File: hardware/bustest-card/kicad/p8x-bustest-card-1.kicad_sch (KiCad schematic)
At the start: 8 parts, among them U1 MCP23S17, U2 MCP23S17, U3 MCP23S17, U4 MCP23S17, U5 MCP23S17, U6 74HCT244, U7 74HCT244

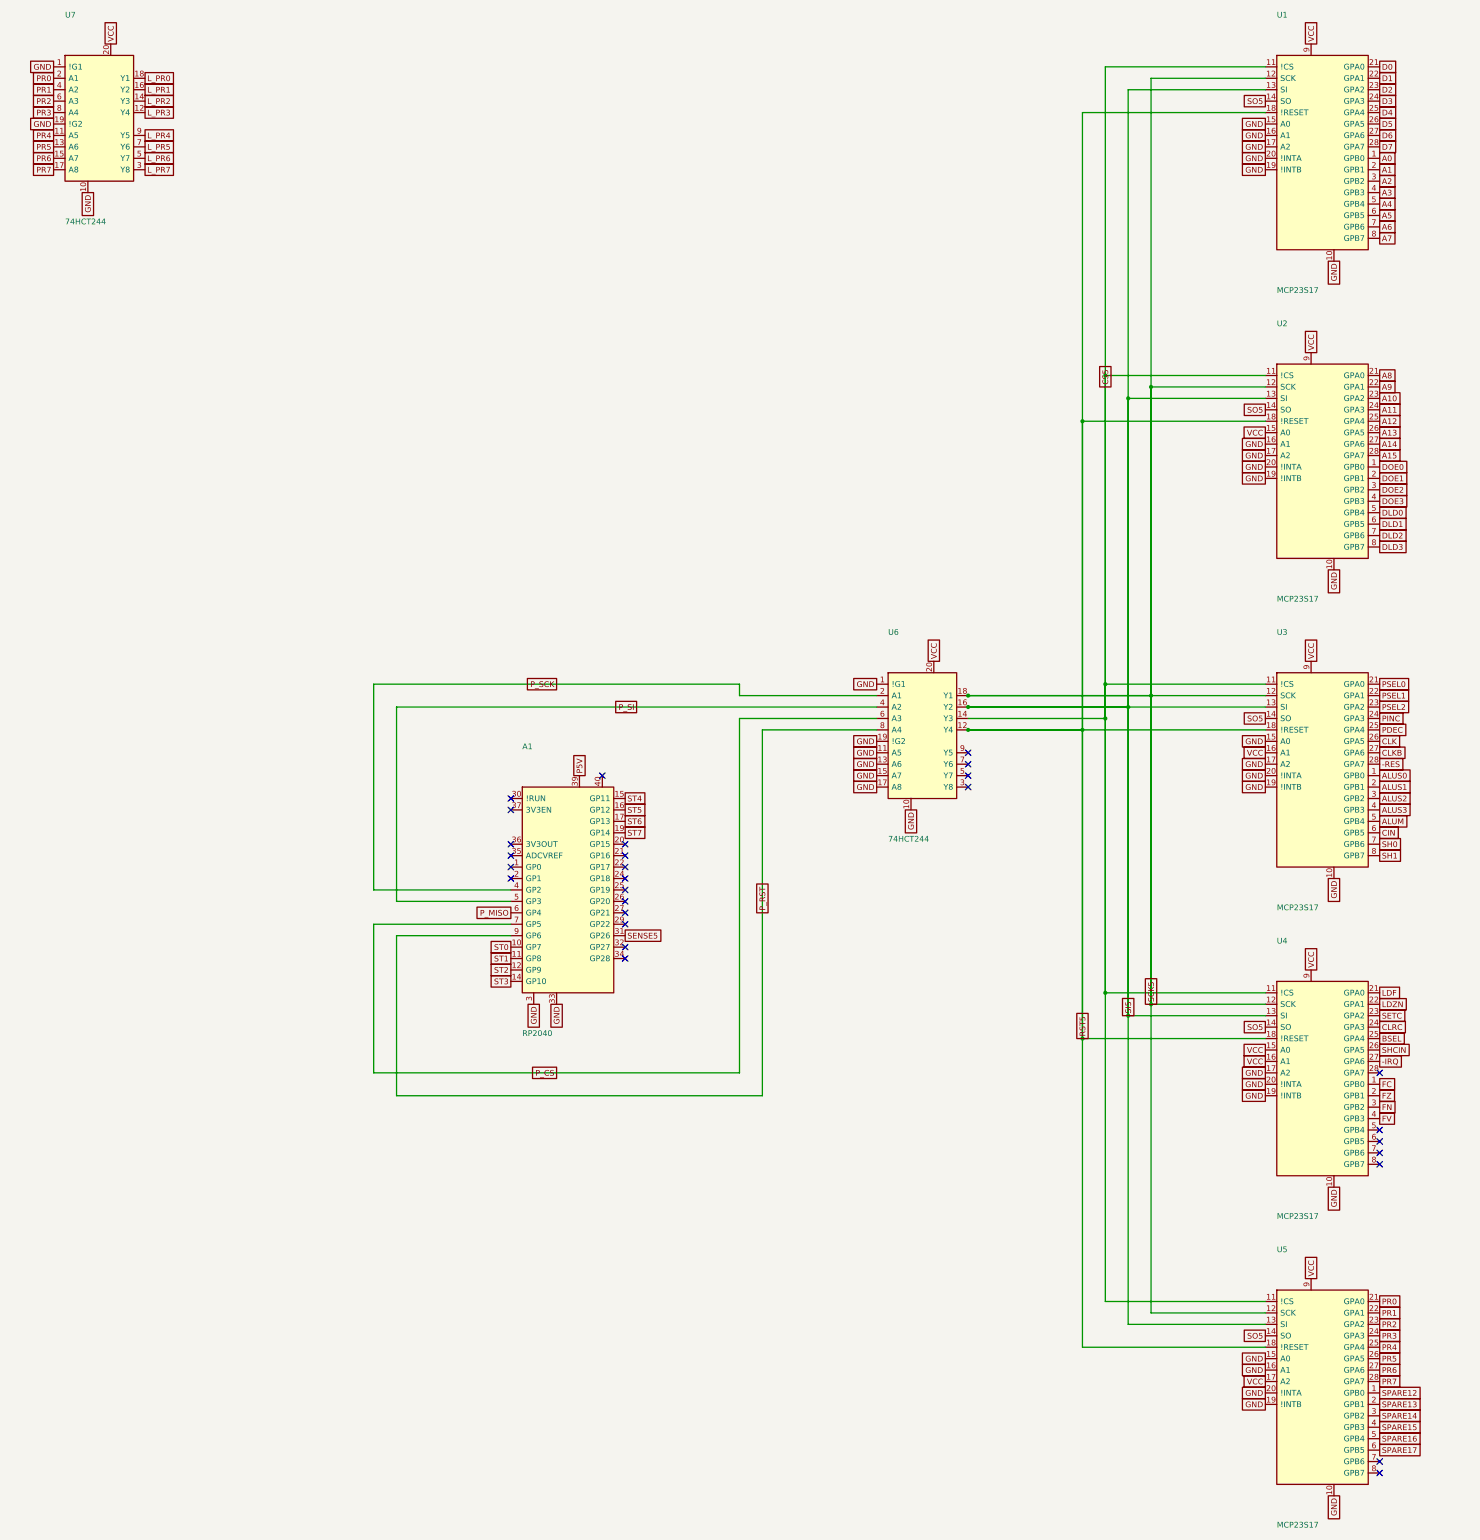
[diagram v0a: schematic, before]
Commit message: feat(sch): draw every P8X card schematic by function
Extend the functional-sheet grouping from the io-card to the control,
regbank, alu, memory, cf, ps2 and bustest cards. functional_sheets now
attaches unnamed glue gates, LEDs, resistors and connectors to the block
they share the most local nets with, so each block lists only its main
parts. A net with two or more pins on a sheet is now wired there even if
it continues elsewhere (its global name label rides on the wire), and
every wire is oriented by drawing side. The regbank gets one pointer per
sheet; the ps2 latches share a sheet with the AVR so the mailbox bus is
drawn. The bustest probe resistors use a straight-order RNISO8DSTR
drawing (the reversed B side forced every wire to cross and the sheet
fell back to labels). build_sch.sh now shows ELK fallbacks and clears old
numbered sheets before a build. All eight netlists match the boards,
ERC 0 errors; the boards change only in footprint link paths.

Co-Authored-By: Claude Opus 5.5 <noreply@anthropic.com>
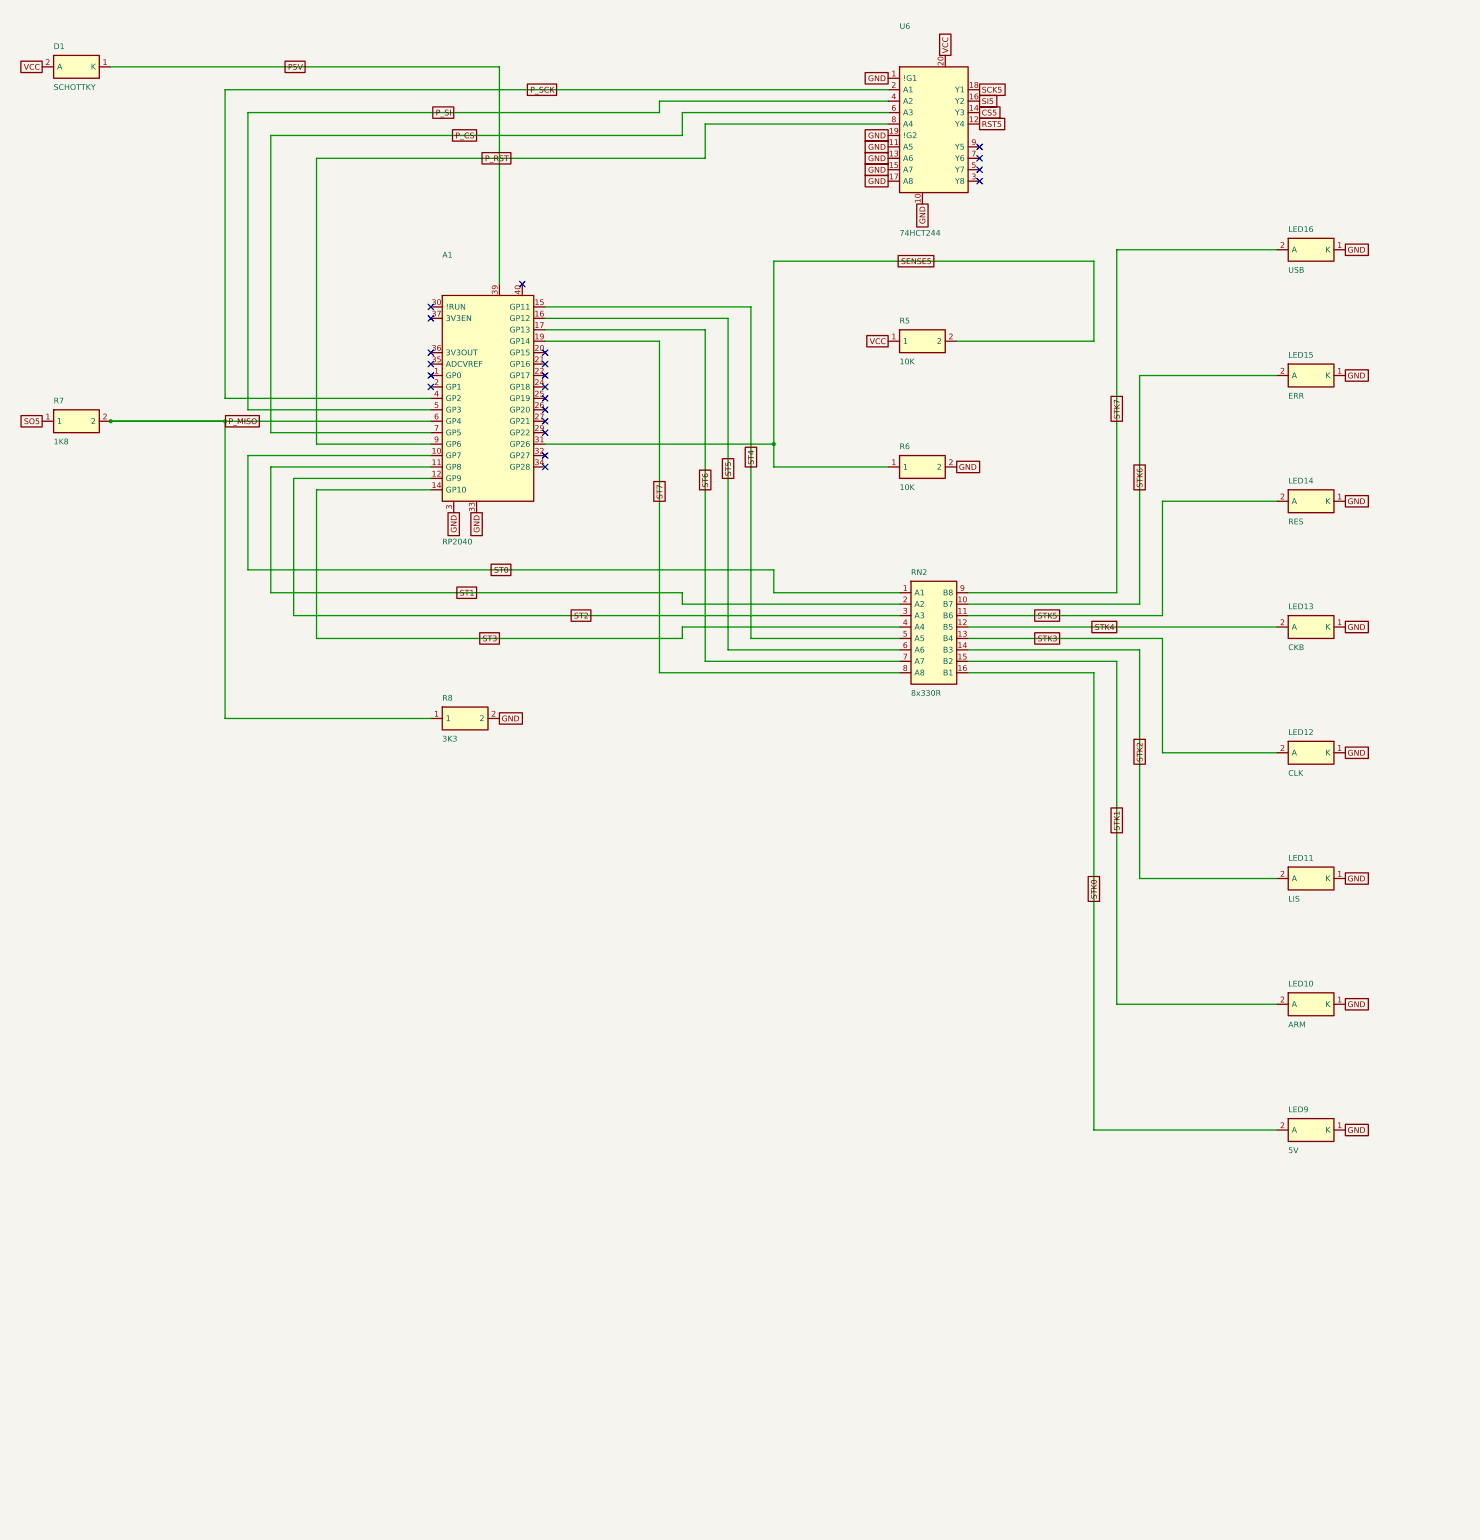
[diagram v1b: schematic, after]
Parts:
- removed U1, U2, U3, U4, U5: MCP23S17, Package_DIP:DIP-28_W7.62mm, symbol p8x:MCP23S17
- removed U7: 74HCT244, Package_DIP:DIP-20_W7.62mm, symbol p8x:74244
- added D1: SCHOTTKY, LED_THT:LED_D5.0mm, symbol p8x:LED
- added LED10: ARM, LED_THT:LED_D5.0mm, symbol p8x:LED
- added LED11: LIS, LED_THT:LED_D5.0mm, symbol p8x:LED
- added LED12: CLK, LED_THT:LED_D5.0mm, symbol p8x:LED
- added LED13: CKB, LED_THT:LED_D5.0mm, symbol p8x:LED
- added LED14: RES, LED_THT:LED_D5.0mm, symbol p8x:LED
- added LED15: ERR, LED_THT:LED_D5.0mm, symbol p8x:LED
- added LED16: USB, LED_THT:LED_D5.0mm, symbol p8x:LED
- added LED9: 5V, LED_THT:LED_D5.0mm, symbol p8x:LED
- added R5, R6: 10K, Resistor_THT:R_Axial_DIN0207_L6.3mm_D2.5mm_P10.16mm_Horizontal, symbol p8x:RES
- added R7: 1K8, Resistor_THT:R_Axial_DIN0207_L6.3mm_D2.5mm_P10.16mm_Horizontal, symbol p8x:RES
- added R8: 3K3, Resistor_THT:R_Axial_DIN0207_L6.3mm_D2.5mm_P10.16mm_Horizontal, symbol p8x:RES
- added RN2: 8x330R, Package_DIP:DIP-16_W7.62mm, symbol p8x:RNISO8D
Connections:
- net GND: now also LED10.1 (K), LED11.1 (K), LED12.1 (K), LED13.1 (K), LED14.1 (K), LED15.1 (K), LED16.1 (K), LED9.1 (K), R6.2, R8.2
- net P5V: now also D1.1 (K)
- net P_MISO: now also R7.2, R8.1
- net SENSE5: now also R5.2, R6.1
- net SO5: now also R7.1
- net ST0: now also RN2.1 (A1)
- net ST1: now also RN2.2 (A2)
- net ST2: now also RN2.3 (A3)
- net ST3: now also RN2.4 (A4)
- net ST4: now also RN2.5 (A5)
- net ST5: now also RN2.6 (A6)
- net ST6: now also RN2.7 (A7)
- net ST7: now also RN2.8 (A8)
- net VCC: now also D1.2 (A), R5.1
- new net STK0: LED9.2 (A), RN2.16 (B1)
- new net STK1: LED10.2 (A), RN2.15 (B2)
- new net STK2: LED11.2 (A), RN2.14 (B3)
- new net STK3: LED12.2 (A), RN2.13 (B4)
- new net STK4: LED13.2 (A), RN2.12 (B5)
- new net STK5: LED14.2 (A), RN2.11 (B6)
- new net STK6: LED15.2 (A), RN2.10 (B7)
- new net STK7: LED16.2 (A), RN2.9 (B8)
- no-connect marks 28 -> 21
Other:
- moved on the sheet: A1, U6

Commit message: fix(bustest,io): real Pico footprint and a CR2032 holder
The bus test card's Pico was a substituted 2x20 pin header (rows 2.54 mm
apart, odd/even numbering), so a Pico could not have been fitted; it is
now KiCad's Module:RaspberryPi_Pico_Common_THT (rows 17.78 mm, Pico pin
order) and all eight Pico ground pins are netted (only 3 and 33 were).
The io-card's CR2032 sat in a Keystone 3000 footprint, a 12 mm SMD
holder; it is now the through-hole Keystone 103 (20 mm) placed in the
free bottom-right corner beside J3. Both boards re-routed: DRC 0
unconnected, PASS. The remaining substitutions were audited; the open
ones (io-card RNISO8 SIP vs the DIP-16 rule, 8-segment DIP-16
bargraphs, the custom MiniDIN-6) are listed under VERIFY in BACKLOG.md.

Co-Authored-By: Claude Opus 5.5 <noreply@anthropic.com>
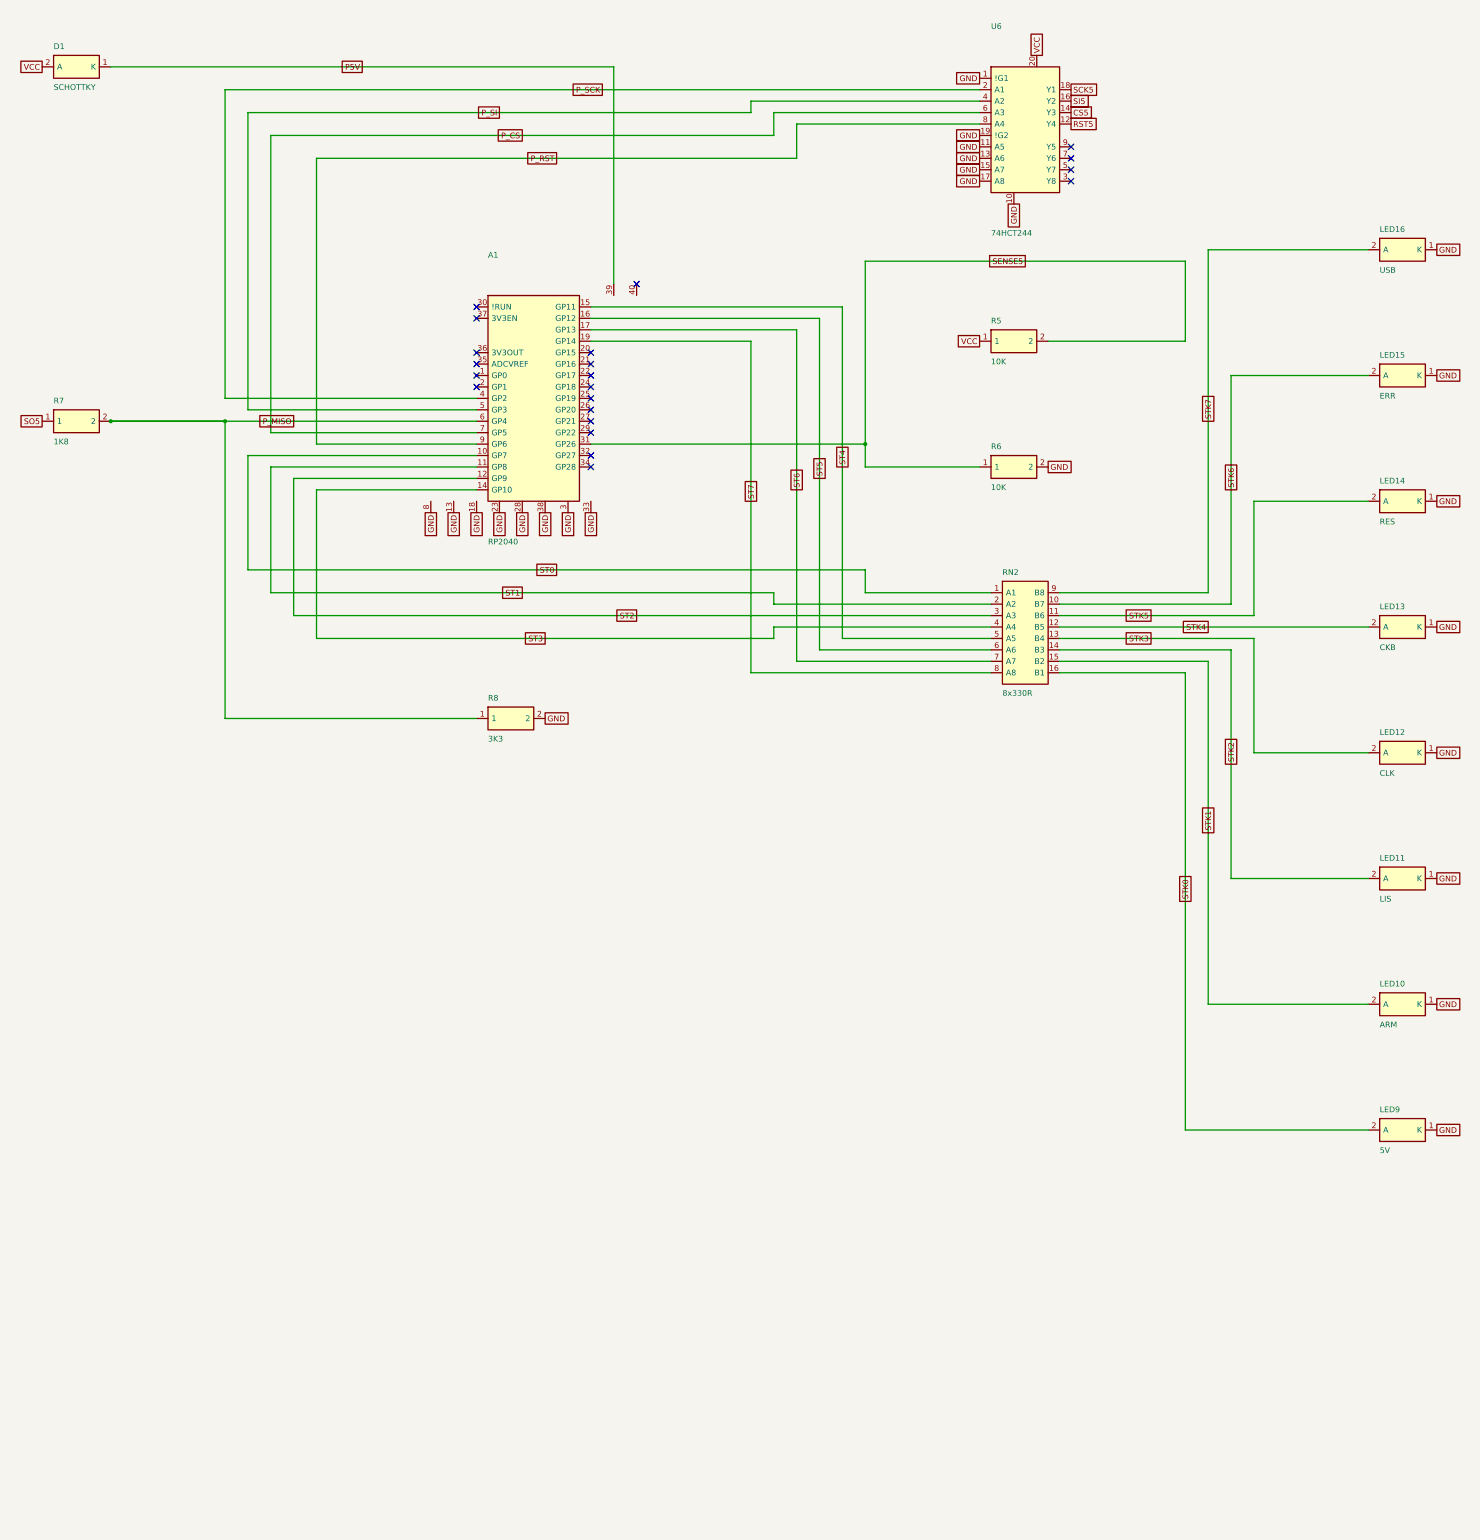
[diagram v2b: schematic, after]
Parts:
- A1: footprint Connector_PinHeader_2.54mm:PinHeader_2x20_P2.54mm_Vertical -> Module:RaspberryPi_Pico_Common_THT
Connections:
- net GND: now also A1.13, A1.18, A1.23, A1.28, A1.38, A1.8
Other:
- moved on the sheet: LED10, LED11, LED12, LED13, LED14, LED15, LED16, LED9, R5, R6, R8, RN2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
